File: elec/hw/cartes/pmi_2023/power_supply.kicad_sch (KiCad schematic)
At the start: 52 parts, among them J5 254, J8 254, Q3 DMP2008UFG-7, SW8 MSS12C02LS-BB2.0, U28 TLV61070A, U29 TLV61070A, U33 TLV61070A, U34 TLV61070A, U35 LDL1117S33R

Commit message: second round of review corrections
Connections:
- net GND: now also SW8.MP
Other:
- moved on the sheet: D7
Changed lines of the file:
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@@
 	)
 	(junction
-		(at 74.93 67.31)
-		(diameter 0)
-		(color 0 0 0 0)
-	)
-	(junction
 		(at 234.95 113.03)
 		(diameter 0)
@@
 	)
 	(junction
+		(at 104.14 57.15)
+		(diameter 0)
+		(color 0 0 0 0)
+	)
+	(junction
 		(at 260.35 66.04)
 		(diameter 0)
@@
 	)
 	(junction
+		(at 76.2 67.31)
+		(diameter 0)
+		(color 0 0 0 0)
+	)
+	(junction
 		(at 48.26 160.02)
 		(diameter 0)
@@
 	)
 	(junction
-		(at 180.34 45.72)
+		(at 69.85 67.31)
 		(diameter 0)
 		(color 0 0 0 0)
 	)
 	(junction
-		(at 222.25 160.02)
+		(at 180.34 45.72)
 		(diameter 0)
 		(color 0 0 0 0)
 	)
 	(junction
-		(at 213.36 63.5)
+		(at 222.25 160.02)
 		(diameter 0)
 		(color 0 0 0 0)
 	)
 	(junction
-		(at 101.6 57.15)
+		(at 213.36 63.5)
 		(diameter 0)
 		(color 0 0 0 0)
@@
 	(wire
 		(pts
-			(xy 78.74 57.15) (xy 101.6 57.15)
+			(xy 78.74 57.15) (xy 104.14 57.15)
 		)
 		(stroke
@@
 	(wire
 		(pts
-			(xy 101.6 67.31) (xy 101.6 66.04)
+			(xy 104.14 67.31) (xy 104.14 66.04)
 		)
 		(stroke
@@
 	(wire
 		(pts
+			(xy 69.85 67.31) (xy 76.2 67.31)
+		)
+		(stroke
+			(width 0)
+			(type default)
+		)
+	)
+	(wire
+		(pts
 			(xy 205.74 30.48) (xy 205.74 34.29)
 		)
@@
 	(wire
 		(pts
+			(xy 69.85 62.23) (xy 69.85 67.31)
+		)
+		(stroke
+			(width 0)
+			(type default)
+		)
+	)
+	(wire
+		(pts
 			(xy 48.26 179.07) (xy 60.96 179.07)
 		)
@@
 	(wire
 		(pts
-			(xy 74.93 67.31) (xy 101.6 67.31)
-		)
-		(stroke
-			(width 0)
-			(type default)
-		)
-	)
-	(wire
-		(pts
 			(xy 260.35 144.78) (xy 262.89 144.78)
 		)
@@
 	(wire
 		(pts
-			(xy 101.6 57.15) (xy 105.41 57.15)
-		)
-		(stroke
-			(width 0)
-			(type default)
-		)
-	)
-	(wire
-		(pts
 			(xy 15.24 15.24) (xy 15.24 33.02)
 		)
@@
 	(wire
 		(pts
-			(xy 77.47 57.15) (xy 78.74 57.15)
-		)
-		(stroke
-			(width 0)
-			(type default)
-		)
-	)
-	(wire
-		(pts
 			(xy 91.44 133.35) (xy 91.44 138.43)
 		)
@@
 	(wire
 		(pts
+			(xy 76.2 67.31) (xy 104.14 67.31)
+		)
+		(stroke
+			(width 0)
+			(type default)
+		)
+	)
+	(wire
+		(pts
+			(xy 104.14 57.15) (xy 105.41 57.15)
+		)
+		(stroke
+			(width 0)
+			(type default)
+		)
+	)
+	(wire
+		(pts
 			(xy 226.06 134.62) (xy 231.14 134.62)
 		)
@@
 	(wire
 		(pts
-			(xy 68.58 67.31) (xy 74.93 67.31)
+			(xy 68.58 67.31) (xy 69.85 67.31)
 		)
 		(stroke
@@
 	(wire
 		(pts
-			(xy 101.6 57.15) (xy 101.6 58.42)
+			(xy 104.14 57.15) (xy 104.14 58.42)
 		)
 		(stroke
@@
 	(symbol
 		(lib_id "cocotter_diodes:green_led_0603")
-		(at 101.6 62.23 90)
+		(at 104.14 62.23 90)
 		(unit 1)
 		(exclude_from_sim no)
@@
 		(fields_autoplaced yes)
 		(property "Reference" "D7"
-			(at 105.41 62.5474 90)
+			(at 107.95 62.5474 90)
 			(effects
 				(font
@@
 		)
 		(property "Value" "green, 0603"
-			(at 104.14 62.23 0)
+			(at 106.68 62.23 0)
 			(effects
 				(font
@@
 		)
 		(property "Footprint" "cocotter_diodes:LED_0603_1608Metric"
-			(at 101.6 62.23 0)
+			(at 104.14 62.23 0)
 			(effects
 				(font
@@
 		)
 		(property "Datasheet" "~"
-			(at 101.6 62.23 0)
+			(at 104.14 62.23 0)
 			(effects
 				(font
@@
 		)
 		(property "Description" "Light emitting diode, Green, Vf=[2V; 2.4V]"
-			(at 101.6 62.23 0)
+			(at 104.14 62.23 0)
 			(effects
 				(font
@@
 		)
 		(property "DIGIKEY_REF" "3147-B19Y1UYG-20C000313U1930CT-ND"
-			(at 101.6 62.23 0)
+			(at 104.14 62.23 0)
 			(effects
 				(font
@@
 		)
 		(property "MOUSER_REF" "710-150060VS55040"
-			(at 101.6 62.23 0)
+			(at 104.14 62.23 0)
 			(effects
 				(font
@@
 		)
 		(property "JLCPCB Part #" "C22371299"
-			(at 105.41 65.0874 90)
+			(at 107.95 65.0874 90)
 			(effects
 				(font
@@
 	(symbol
 		(lib_id "cocotter_connectors:MSS12C02LS-BB2.0")
-		(at 74.93 62.23 270)
+		(at 76.2 62.23 270)
 		(unit 1)
 		(exclude_from_sim no)
@@
 		(on_board yes)
 		(dnp no)
-		(fields_autoplaced yes)
 		(property "Reference" "SW8"
-			(at 80.01 60.9599 90)
+			(at 81.28 60.9599 90)
 			(effects
 				(font
@@
 		)
 		(property "Value" "MSS12C02LS-BB2.0"
-			(at 80.01 63.4999 90)
+			(at 81.28 63.4999 90)
 			(effects
 				(font
@@
 		)
 		(property "Footprint" "cocotter_connectors:MSS12C02LS-BB2.0"
-			(at 74.93 62.23 0)
+			(at 76.2 62.23 0)
 			(effects
 				(font
@@
 		)
 		(property "Datasheet" "https://www.mouser.fr/datasheet/2/910/606_MSS614-1571571.pdf"
-			(at 69.85 62.23 0)
+			(at 71.12 62.23 0)
 			(effects
 				(font
@@
 		)
 		(property "Description" "100mA max, 12Vdc, 10000 cycles"
-			(at 74.93 62.23 0)
+			(at 76.2 62.23 0)
 			(effects
 				(font
@@
 		)
 		(property "JLCPCB Part #" "C3008585"
-			(at 69.85 60.96 0)
+			(at 71.12 60.96 0)
 			(effects
 				(font
@@
 		(pin "B"
 		)
+		(pin "MP"
+		)
 		(instances

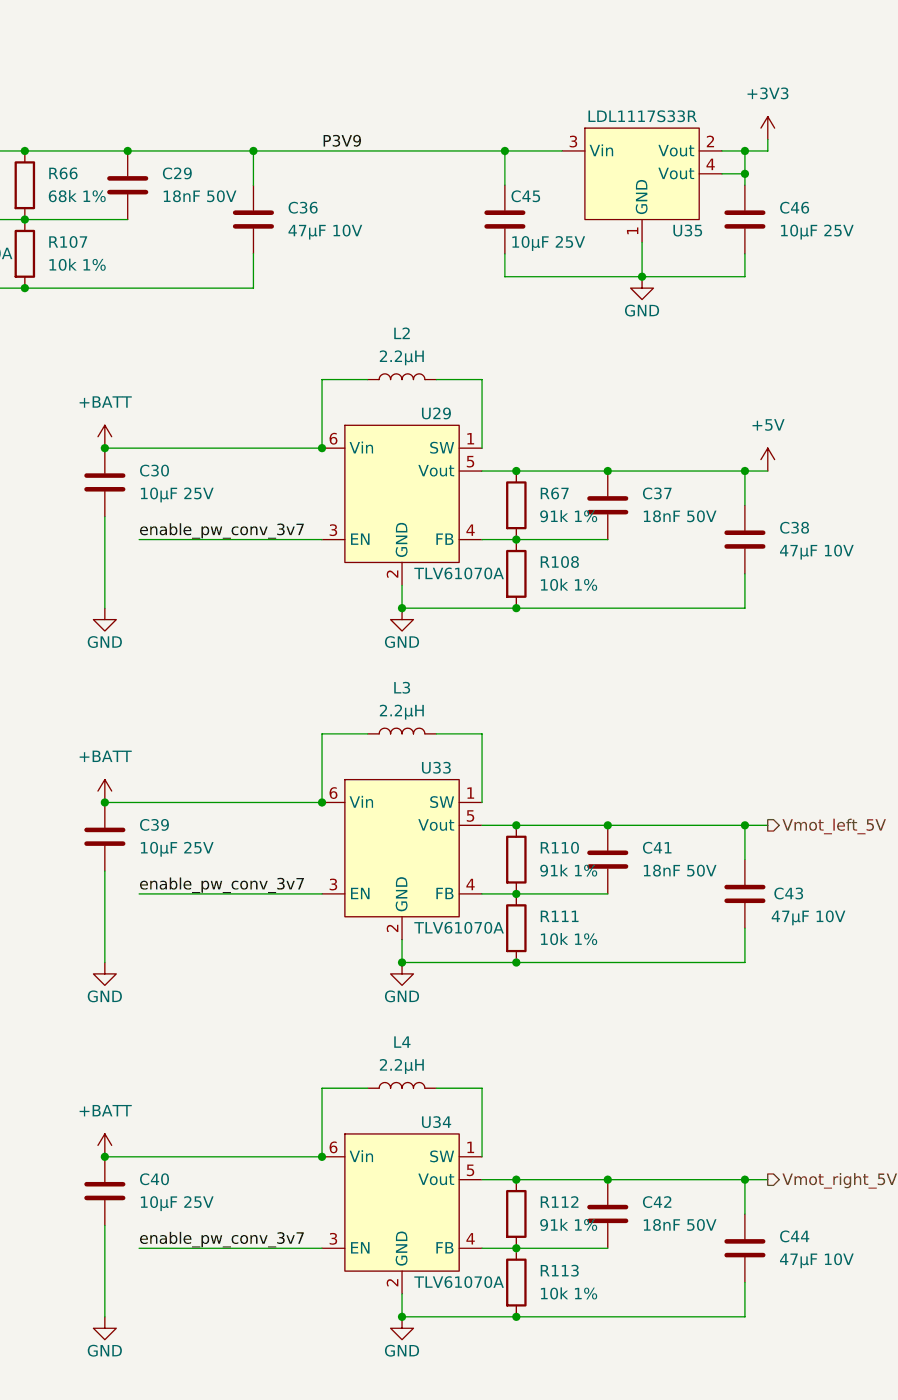
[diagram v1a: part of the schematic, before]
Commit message: 18nF capacitors replaced by 2nF
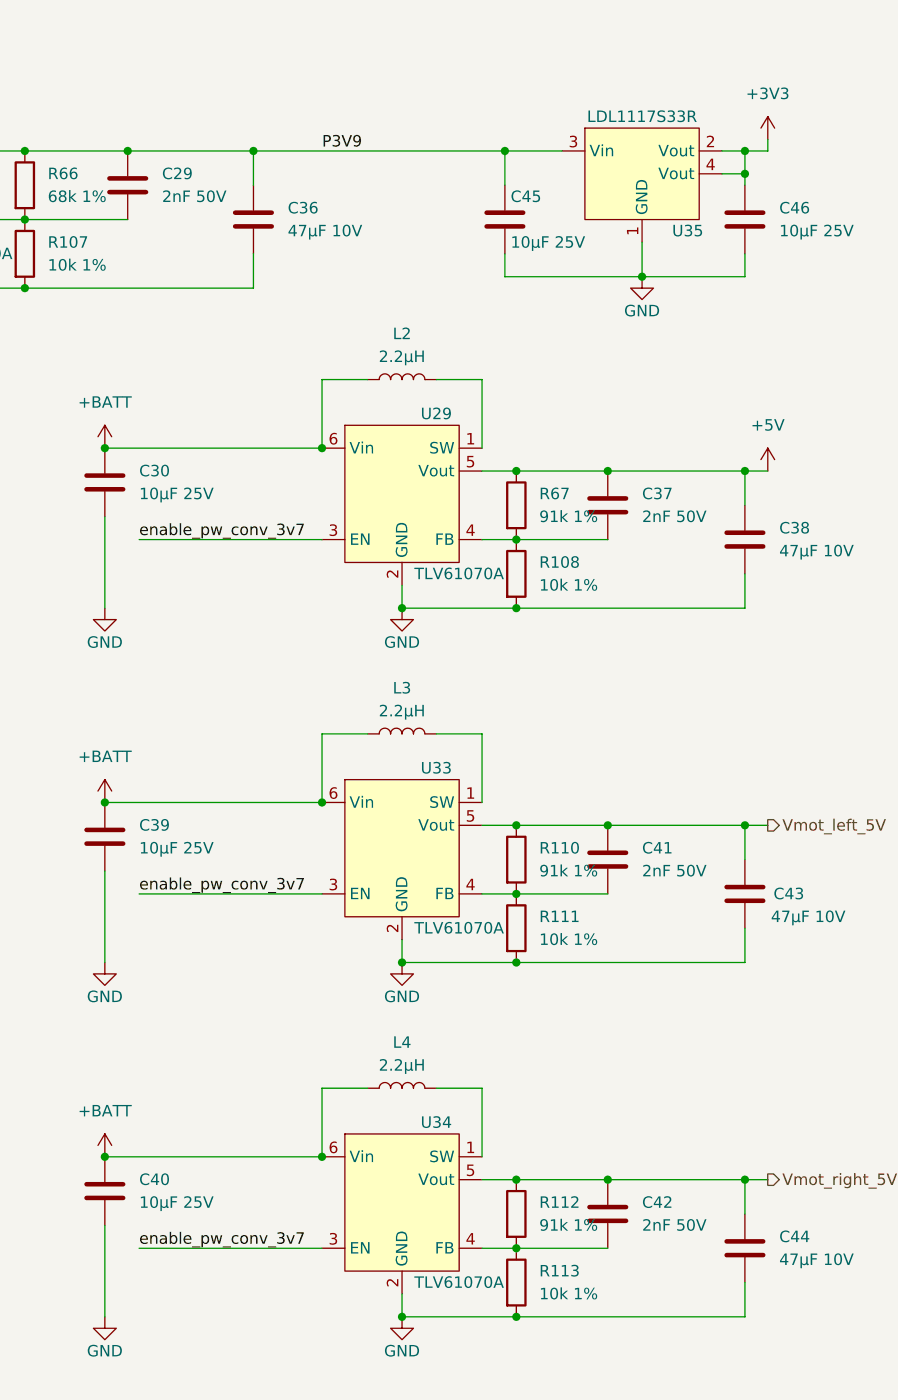
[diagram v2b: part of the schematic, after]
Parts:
- C29, C37, C41, C42: value 18nF 50V -> 2nF 50V; symbol cocotter_capacitors:C_18nF_50V_0603 -> cocotter_capacitors:C_2nF_50V_0603; JLCPCB Part # C107079 -> C282245; Specification 18nF 50V X7R 0603 -> 2nF 50V X7R 0603
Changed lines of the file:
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@@
 	)
 	(symbol
-		(lib_id "cocotter_capacitors:C_18nF_50V_0603")
+		(lib_id "cocotter_capacitors:C_2nF_50V_0603")
 		(at 245.11 69.85 0)
 		(unit 1)
@@
 		(fields_autoplaced yes)
 		(property "Reference" "C37"
-			(at 248.92 68.58 0)
-			(effects
-				(font
-					(size 1.27 1.27)
-				)
-				(justify left)
-			)
-		)
-		(property "Value" "18nF 50V"
-			(at 248.92 71.12 0)
+			(at 248.92 68.5799 0)
+			(effects
+				(font
+					(size 1.27 1.27)
+				)
+				(justify left)
+			)
+		)
+		(property "Value" "2nF 50V"
+			(at 248.92 71.1199 0)
 			(effects
 				(font
@@
 			)
 		)
-		(property "Specification" "18nF 50V X7R 0603 "
+		(property "Specification" "2nF 50V X7R 0603 "
 			(at 245.11 69.85 0)
 			(effects
@@
 			)
 		)
-		(property "JLCPCB Part #" "C107079 "
+		(property "JLCPCB Part #" "C282245"
 			(at 245.11 69.85 0)
 			(effects
@@
 	)
 	(symbol
-		(lib_id "cocotter_capacitors:C_18nF_50V_0603")
+		(lib_id "cocotter_capacitors:C_2nF_50V_0603")
 		(at 245.11 148.59 0)
 		(unit 1)
@@
 		(fields_autoplaced yes)
 		(property "Reference" "C42"
-			(at 248.92 147.32 0)
-			(effects
-				(font
-					(size 1.27 1.27)
-				)
-				(justify left)
-			)
-		)
-		(property "Value" "18nF 50V"
-			(at 248.92 149.86 0)
+			(at 248.92 147.3199 0)
+			(effects
+				(font
+					(size 1.27 1.27)
+				)
+				(justify left)
+			)
+		)
+		(property "Value" "2nF 50V"
+			(at 248.92 149.8599 0)
 			(effects
 				(font
@@
 			)
 		)
-		(property "Specification" "18nF 50V X7R 0603 "
+		(property "Specification" "2nF 50V X7R 0603 "
 			(at 245.11 148.59 0)
 			(effects
@@
 			)
 		)
-		(property "JLCPCB Part #" "C107079 "
+		(property "JLCPCB Part #" "C282245"
 			(at 245.11 148.59 0)
 			(effects
@@
 	)
 	(symbol
-		(lib_id "cocotter_capacitors:C_18nF_50V_0603")
+		(lib_id "cocotter_capacitors:C_2nF_50V_0603")
 		(at 245.11 109.22 0)
 		(unit 1)
@@
 		(fields_autoplaced yes)
 		(property "Reference" "C41"
-			(at 248.92 107.95 0)
-			(effects
-				(font
-					(size 1.27 1.27)
-				)
-				(justify left)
-			)
-		)
-		(property "Value" "18nF 50V"
-			(at 248.92 110.49 0)
+			(at 248.92 107.9499 0)
+			(effects
+				(font
+					(size 1.27 1.27)
+				)
+				(justify left)
+			)
+		)
+		(property "Value" "2nF 50V"
+			(at 248.92 110.4899 0)
 			(effects
 				(font
@@
 			)
 		)
-		(property "Specification" "18nF 50V X7R 0603 "
+		(property "Specification" "2nF 50V X7R 0603 "
 			(at 245.11 109.22 0)
 			(effects
@@
 			)
 		)
-		(property "JLCPCB Part #" "C107079 "
+		(property "JLCPCB Part #" "C282245"
 			(at 245.11 109.22 0)
 			(effects
@@
 	)
 	(symbol
-		(lib_id "cocotter_capacitors:C_18nF_50V_0603")
+		(lib_id "cocotter_capacitors:C_2nF_50V_0603")
 		(at 191.77 34.29 0)
 		(unit 1)
@@
 		(fields_autoplaced yes)
 		(property "Reference" "C29"
-			(at 195.58 33.02 0)
-			(effects
-				(font
-					(size 1.27 1.27)
-				)
-				(justify left)
-			)
-		)
-		(property "Value" "18nF 50V"
-			(at 195.58 35.56 0)
+			(at 195.58 33.0199 0)
+			(effects
+				(font
+					(size 1.27 1.27)
+				)
+				(justify left)
+			)
+		)
+		(property "Value" "2nF 50V"
+			(at 195.58 35.5599 0)
 			(effects
 				(font
@@
 			)
 		)
-		(property "Specification" "18nF 50V X7R 0603 "
+		(property "Specification" "2nF 50V X7R 0603 "
 			(at 191.77 34.29 0)
 			(effects
@@
 			)
 		)
-		(property "JLCPCB Part #" "C107079 "
+		(property "JLCPCB Part #" "C282245"
 			(at 191.77 34.29 0)
 			(effects

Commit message: pmi board V2, ready for review
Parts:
- added R148: 91k 1%, cocotter_resistor:r0603_reflow, symbol cocotter_resistors:R_91k_0603_1%
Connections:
- net +BATT: now also SW8.A; no longer R114.1
- net GND: now also R114.2, R148.2; no longer D7.C, SW8.B
- net enable_pw_conv_3v7: now also SW8.B, R148.1; no longer R114.2, SW8.A
- new net: D7.C, R114.1
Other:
- note removed: "ajouter CTN NRNE104H3435B2H pour BQ25308. plus 5 pastilles pour pogo pin >3.5A ref 0908-0-15-20-75-14-11-0: vbatt"
- moved on the sheet: D7, Q3, R114, R65, SW8A, TP11, TP9

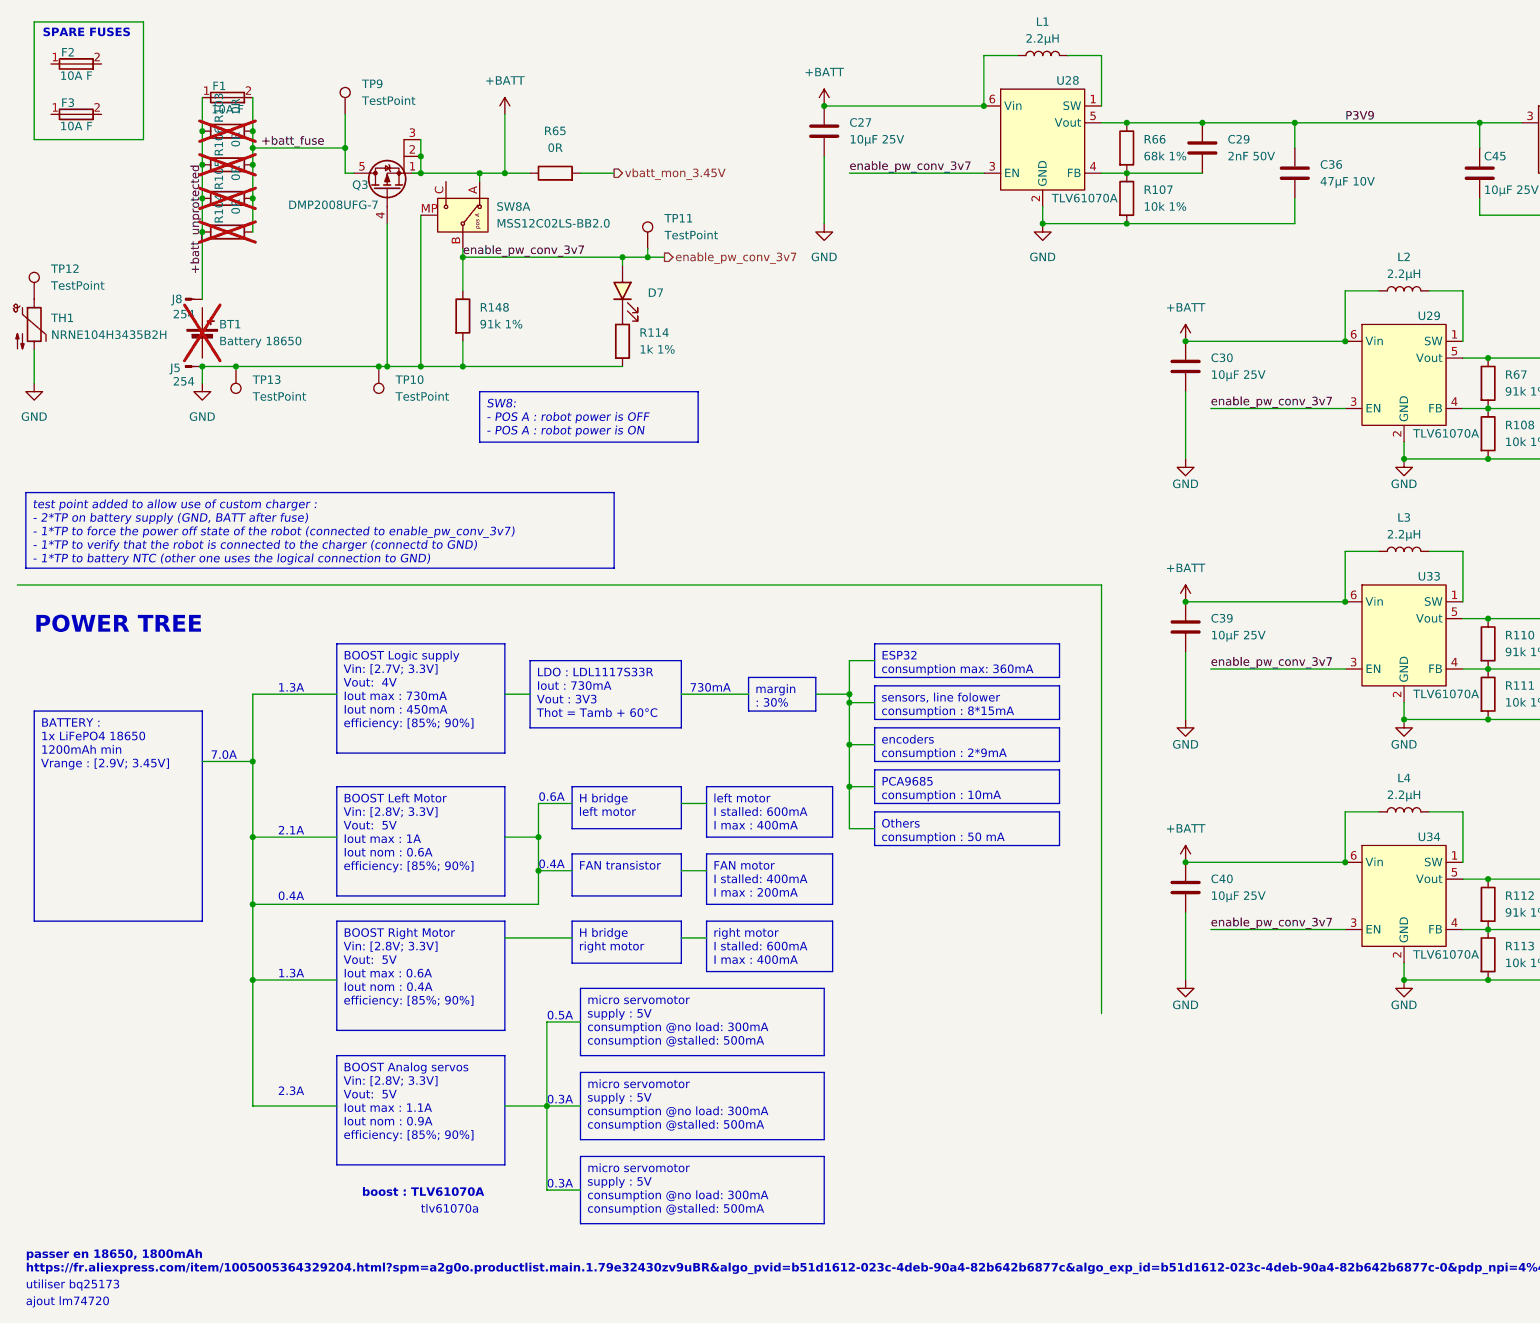
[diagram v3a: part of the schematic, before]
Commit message: pmi : replaced accelerometer and gyroscope with BMI088
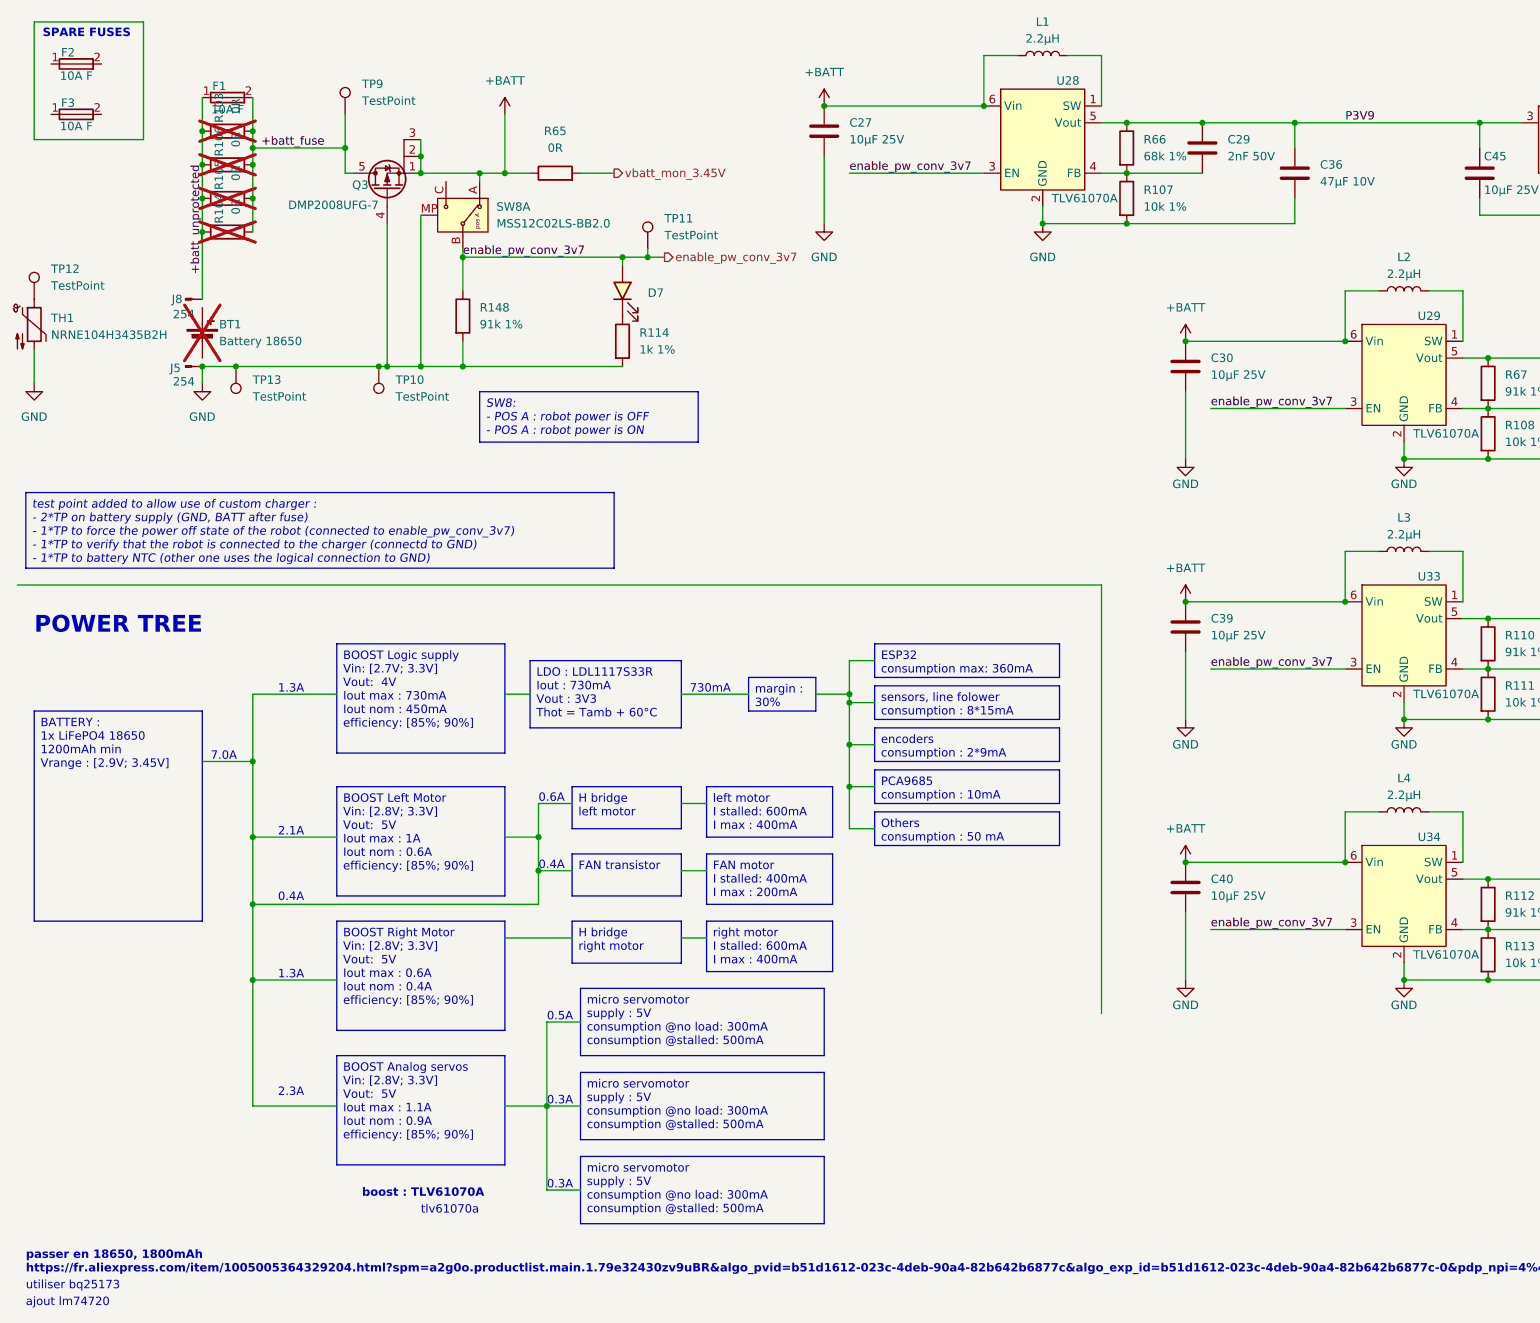
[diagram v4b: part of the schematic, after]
